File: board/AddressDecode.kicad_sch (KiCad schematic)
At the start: 22 parts, among them U10 74LS154, U11 74F00, U12 74F86, U13 74F08, U14 74F32, U15 74F30, U16 74LS260, U17 74LS154, U18 74F02, U25 74LS260, U46 74F32, U51 74F02

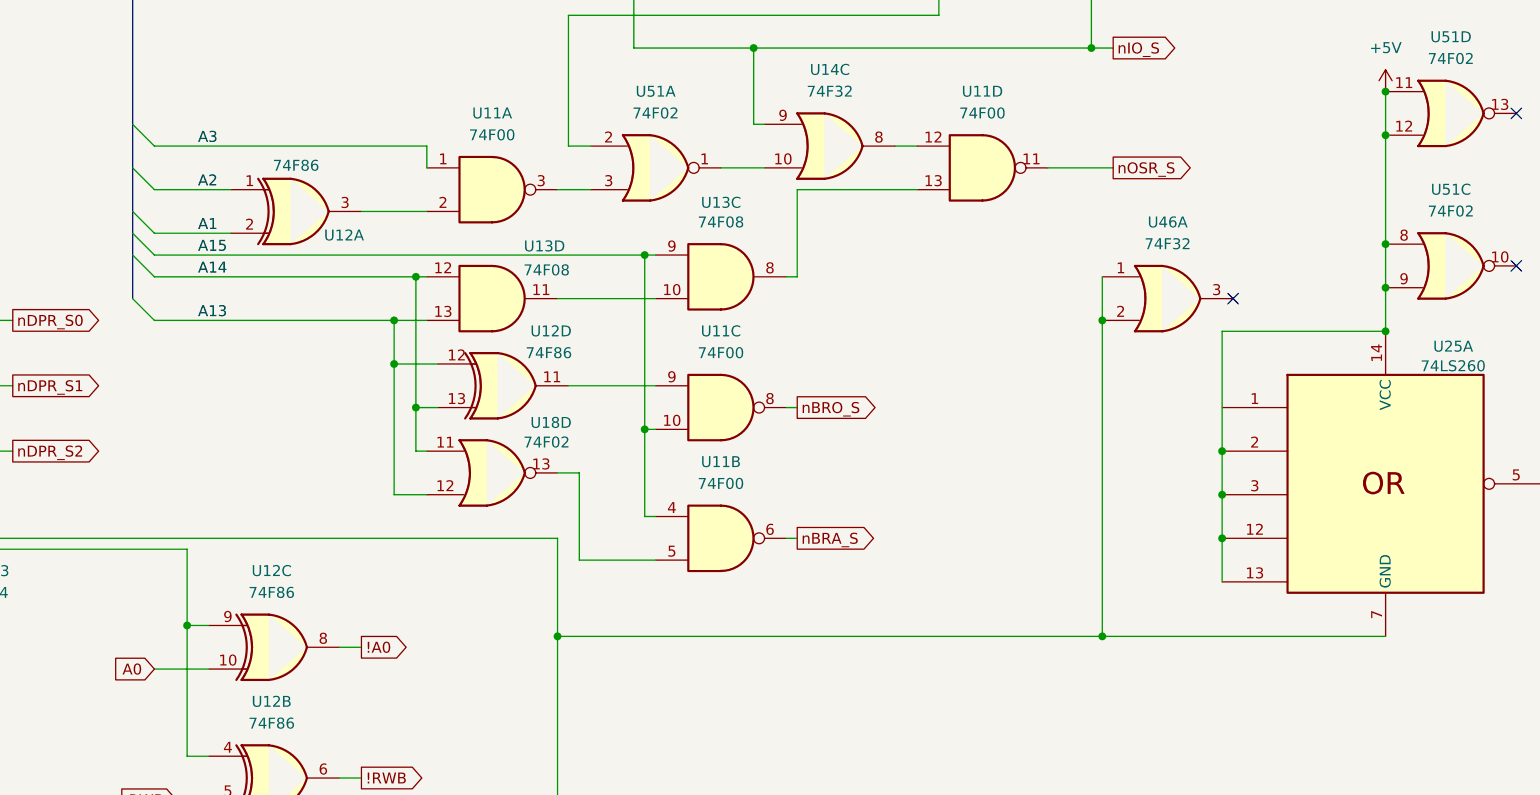
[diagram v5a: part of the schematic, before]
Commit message: Board version 0.6F, moving stuff around and updating the silkscreen to be more consistent.
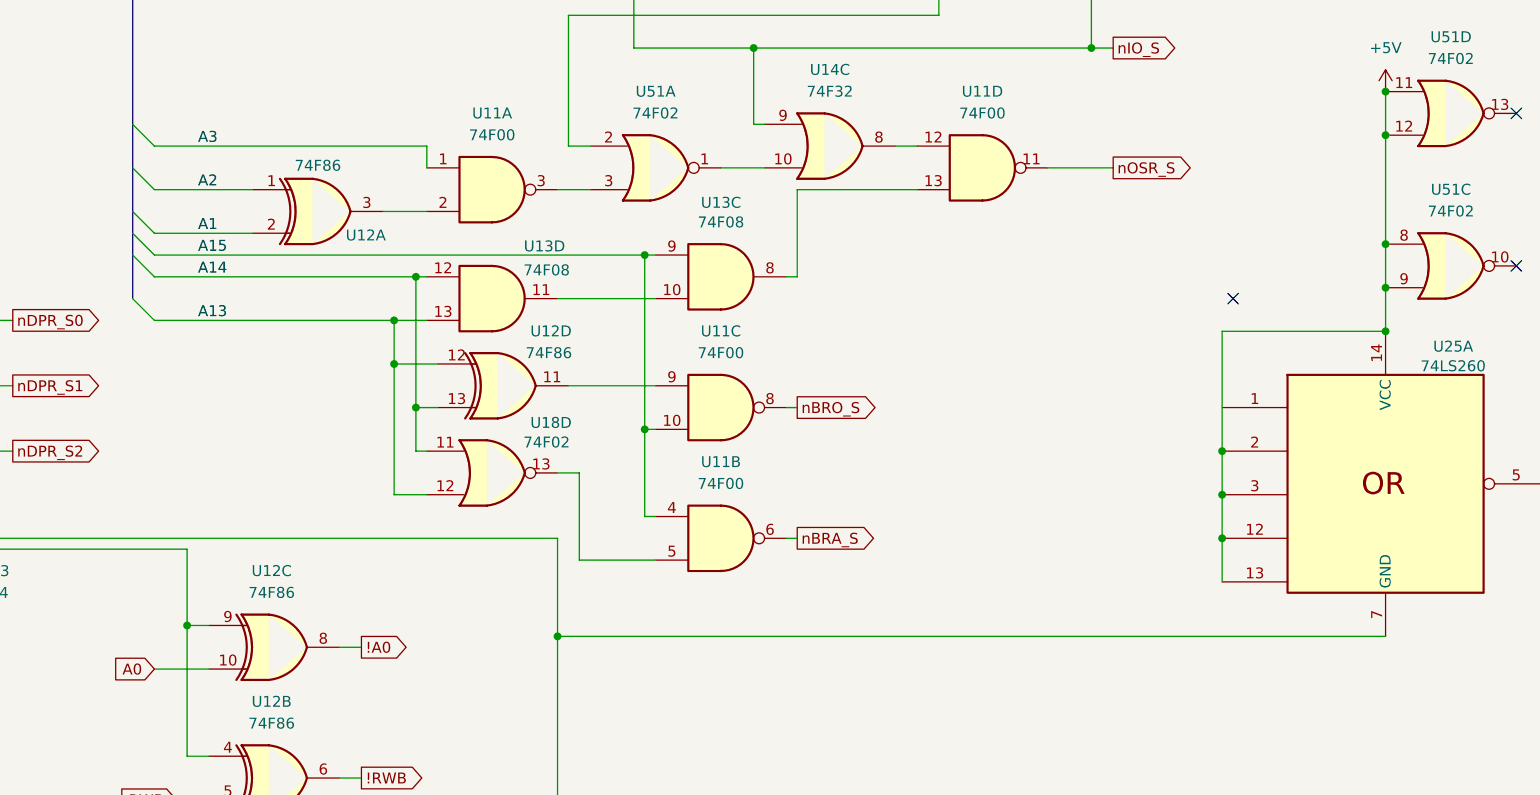
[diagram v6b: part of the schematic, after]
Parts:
- removed U46: 74F32, Package_DIP:DIP-14_W7.62mm_Socket_LongPads, symbol 74xx:74LS32
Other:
- moved on the sheet: U12A
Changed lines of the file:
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@@
 	(title_block
 		(title "Address Decode Logic")
-		(date "2024-10-21")
-		(rev "0.5A")
+		(date "2024-11-21")
+		(rev "0.5C")
 		(company "Data Tuning")
 		(comment 1 "Hydra 16")
@@
 	)
 	(junction
-		(at 210.82 163.83)
-		(diameter 0)
-		(color 0 0 0 0)
-	)
-	(junction
 		(at 160.02 30.48)
 		(diameter 0)
@@
 	)
 	(junction
-		(at 210.82 127)
-		(diameter 0)
-		(color 0 0 0 0)
-	)
-	(junction
 		(at 138.43 21.59)
 		(diameter 0)
@@
 	(wire
 		(pts
-			(xy 100.33 116.84) (xy 109.22 116.84)
+			(xy 100.33 116.84) (xy 111.76 116.84)
 		)
 		(stroke
@@
 	(wire
 		(pts
-			(xy 147.32 163.83) (xy 210.82 163.83)
-		)
-		(stroke
-			(width 0)
-			(type default)
-		)
-	)
-	(wire
-		(pts
 			(xy 248.92 53.34) (xy 246.38 53.34)
 		)
@@
 	(wire
 		(pts
-			(xy 210.82 127) (xy 210.82 163.83)
-		)
-		(stroke
-			(width 0)
-			(type default)
-		)
-	)
-	(wire
-		(pts
 			(xy 118.11 38.1) (xy 120.65 38.1)
 		)
@@
 	(wire
 		(pts
-			(xy 210.82 127) (xy 210.82 121.92)
-		)
-		(stroke
-			(width 0)
-			(type default)
-		)
-	)
-	(wire
-		(pts
 			(xy 209.55 58.42) (xy 209.55 95.25)
 		)
@@
 	(wire
 		(pts
-			(xy 210.82 163.83) (xy 243.84 163.83)
+			(xy 147.32 163.83) (xy 243.84 163.83)
 		)
 		(stroke
@@
 	(wire
 		(pts
-			(xy 124.46 114.3) (xy 132.08 114.3)
+			(xy 127 114.3) (xy 132.08 114.3)
 		)
 		(stroke
@@
 	(wire
 		(pts
-			(xy 100.33 111.76) (xy 109.22 111.76)
+			(xy 100.33 111.76) (xy 111.76 111.76)
 		)
 		(stroke
@@
 	(symbol
 		(lib_id "74xx:74LS86")
-		(at 116.84 114.3 0)
+		(at 119.38 114.3 0)
 		(unit 1)
 		(exclude_from_sim no)
@@
 		(dnp no)
 		(property "Reference" "U12"
-			(at 122.428 117.094 0)
+			(at 124.968 117.094 0)
 			(effects
 				(font
@@
 		)
 		(property "Value" "74F86"
-			(at 116.84 108.966 0)
+			(at 119.38 108.966 0)
 			(effects
 				(font
@@
 		)
 		(property "Footprint" "Package_DIP:DIP-14_W7.62mm_Socket_LongPads"
-			(at 116.84 114.3 0)
+			(at 119.38 114.3 0)
 			(effects
 				(font
@@
 		)
 		(property "Datasheet" "74xx/74ls86.pdf"
-			(at 116.84 114.3 0)
+			(at 119.38 114.3 0)
 			(effects
 				(font
@@
 		)
 		(property "Description" "Quad 2-input XOR"
-			(at 116.84 114.3 0)
+			(at 119.38 114.3 0)
 			(effects
 				(font
@@
 					(unit 1)
 				)
-			)
-		)
-	)
-	(symbol
-		(lib_id "74xx:74LS32")
-		(at 218.44 124.46 0)
-		(unit 1)
-		(exclude_from_sim no)
-		(in_bom yes)
-		(on_board yes)
-		(dnp no)
-		(fields_autoplaced yes)
-		(property "Reference" "U46"
-			(at 218.44 115.57 0)
-			(effects
-				(font
-					(size 1.27 1.27)
-				)
-			)
-		)
-		(property "Value" "74F32"
-			(at 218.44 118.11 0)
-			(effects
-				(font
-					(size 1.27 1.27)
-				)
-			)
-		)
-		(property "Footprint" "Package_DIP:DIP-14_W7.62mm_Socket_LongPads"
-			(at 218.44 124.46 0)
-			(effects
-				(font
-					(size 1.27 1.27)
-				)
-				(hide yes)
-			)
-		)
-		(property "Datasheet" "http://www.ti.com/lit/gpn/sn74LS32"
-			(at 218.44 124.46 0)
-			(effects
-				(font
-					(size 1.27 1.27)
-				)
-				(hide yes)
-			)
-		)
-		(property "Description" "Quad 2-input OR"
-			(at 218.44 124.46 0)
-			(effects
-				(font
-					(size 1.27 1.27)
-				)
-				(hide yes)
-			)
-		)
-		(pin "9"
-		)
-		(pin "7"
-		)
-		(pin "11"
-		)
-		(pin "8"
-		)
-		(pin "12"
-		)
-		(pin "1"
-		)
-		(pin "2"
-		)
-		(pin "4"
-		)
-		(pin "5"
-		)
-		(pin "14"
-		)
-		(pin "3"
-		)
-		(pin "10"
-		)
-		(pin "13"
-		)
-		(pin "6"
-		)
-		(instances
-			(project "hydra-16"
-				(path "/ef29fc71-3fec-48b5-8a1a-46bee537a98c/e447d2ea-fe27-4cfd-bb5f-eaf105a9519f"
-					(reference "U46")
-					(unit 1)
-				)

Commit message: 0.8 Not sure what state it is in
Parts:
- removed C68: 104, Capacitor_THT:C_Disc_D5.0mm_W2.5mm_P5.00mm, symbol Device:C_Small
- removed unit 2 of U12
- removed U17: 74LS154, Package_DIP:DIP-24_W15.24mm_Socket_LongPads, symbol 74xx_IEEE:74154
- removed U51: 74F02, Package_DIP:DIP-14_W7.62mm_Socket_LongPads, symbol 74xx:7402
- added U17: 7404, Package_DIP:DIP-14_W7.62mm_Socket_LongPads, symbol 74xx_IEEE:7404
- added U51: 74F138, Package_DIP:DIP-16_W7.62mm_Socket_LongPads, symbol 74xx:74HC138
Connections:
- net !A0: now also U17.2; no longer U12.8
- net !RWB: now also U17.4
- net +5V: now also C33.2, U51.16 (VCC), U51.6 (E2); no longer C33.1, U12.9, U25.12, U25.13, U25.2, U25.3
- net A0: now also U17.1, U51.1 (A0); no longer U12.10
- net A1: now also U51.2 (A1)
- net A13: now also U13.12, U18.11; no longer U13.13, U18.12
- net A14: now also U13.13, U18.12; no longer U13.12, U18.11
- net A2: now also U12.9, U51.3 (A2)
- net A3: now also U12.10
- net GND: now also C33.1, U25.12, U25.13, U25.3, U17.14 (VCC), U17.14 (VCC), U17.7 (GND), U17.7 (GND), U51.8 (GND); no longer C33.2
- net RWB: now also U17.3
- net nIOB0_S: now also U51.15 (~{Y0})
- net nIOB12_S: now also U51.11 (~{Y4})
- net nIOB13_S: now also U51.10 (~{Y5})
- net nIOB14_S: now also U51.9 (~{Y6})
- net nIOB15_S: now also U51.7 (~{Y7})
- net nIOB1_S: now also U51.14 (~{Y1})
- net nIOB2_S: now also U51.13 (~{Y2})
- net nIOB3_S: now also U51.12 (~{Y3})
- net nIOP15_S: now also U25.1
- net nIO_S: now also U51.5 (~{E1})
- net at U14.10: now also U25.5
- net at U11.3: now also U25.2
- new net: U12.8, U51.4 (~{E0})
- no-connect marks 4 -> 0
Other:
- moved on the sheet: C15, C19, C21, U11D, U11E, U14C, U25A, U25B
